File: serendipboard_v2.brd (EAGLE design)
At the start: 34.3 x 56.8 mm, 86 parts, among them IC1 TP4056, IC2 DW01A, IC3 DS3231/SO, J4 USB3076-XX-X_REVC, Q1 FS8205A, Q2 MMBT2222ALT1G, Q3 RUC002N05HZGT116, Q4 DMG3415U, Q5 MMBT2222ALT1G, Q7 RUC002N05HZGT116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

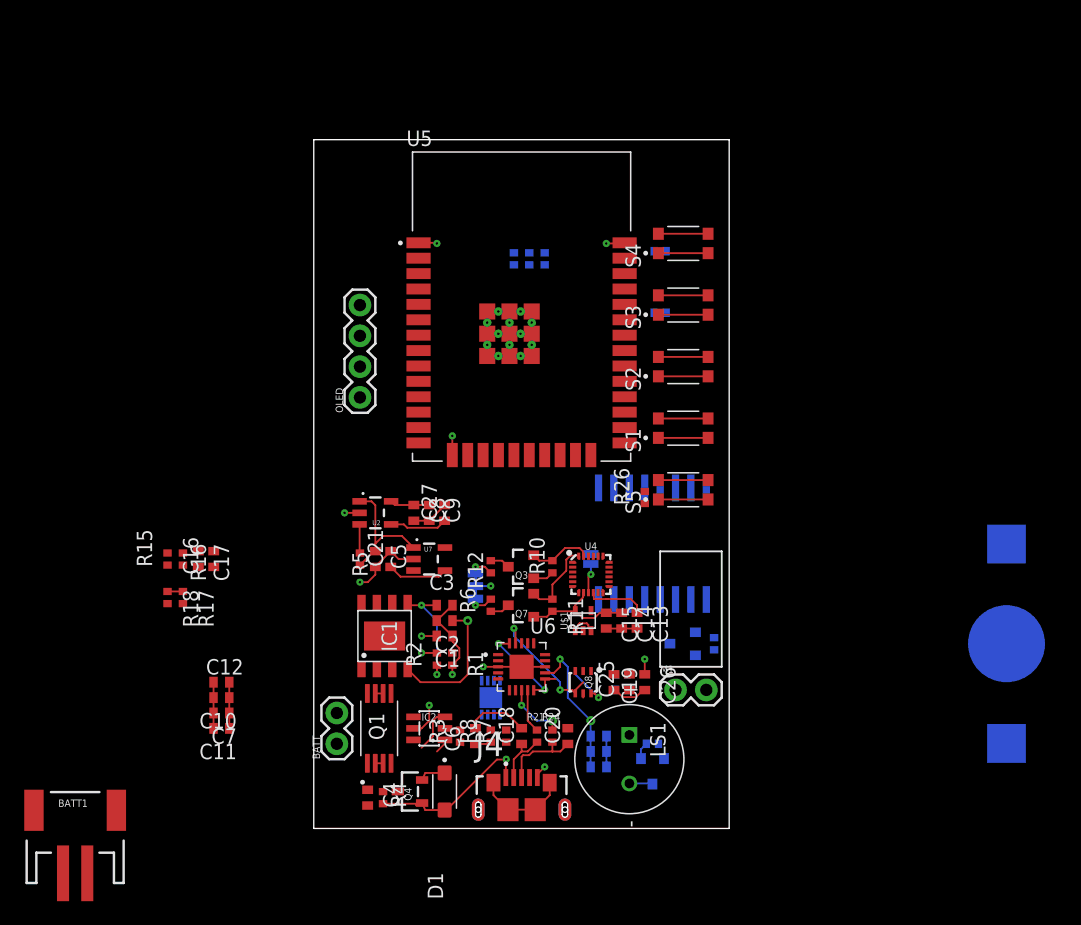
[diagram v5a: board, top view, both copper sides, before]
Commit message: Update serendipboard_v2.brd
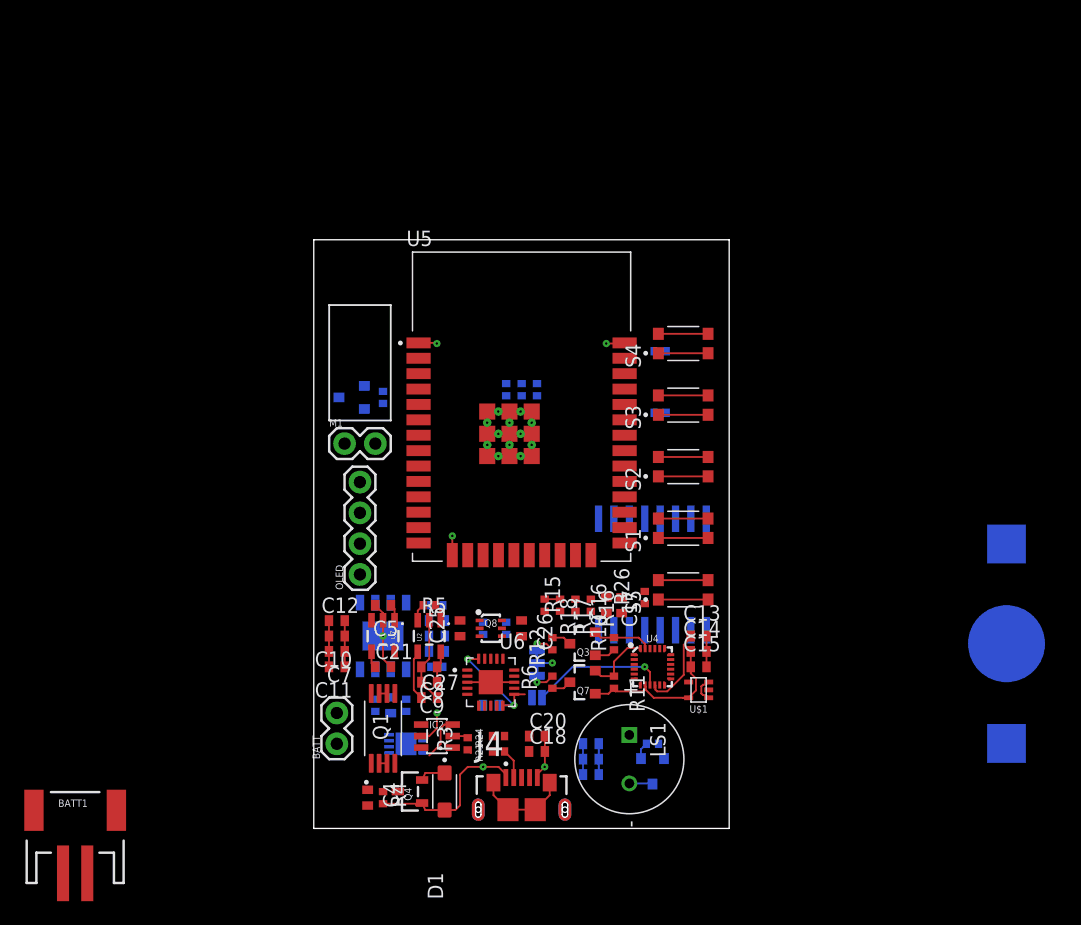
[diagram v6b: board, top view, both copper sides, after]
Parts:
- moved R13 34.0 mm to (5.71, 35.6)
- moved M1 34.0 mm to (2.54, 31.8)
- moved Q5 34.0 mm to (3.17, 35.6)
- moved C16 33.9 mm to (25.4, 18.4)
- moved C17 33.9 mm to (24.1, 18.4)
- moved R15 33.9 mm to (21.6, 18.4)
- moved R16 33.9 mm to (22.9, 18.4)
- moved R17 31.1 mm to (20.3, 18.4)
- moved R18 31.1 mm to (19.1, 18.4)
- moved C27 15.3 mm to (9.53, 10.8), turned to 0 degrees
- moved C25 14.7 mm to (12.1, 16.5)
- moved OLED 14.6 mm to (3.81, 21.0)
- moved C9 14.0 mm to (9.53, 12.1), turned to 180 degrees
- moved C8 12.8 mm to (9.53, 13.3), turned to 180 degrees
- moved R23 12.5 mm to (14.0, 16.5), turned to 270 degrees
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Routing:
- net VBUS: track 37.3 -> 16.9 mm, vias 4 -> 1
- net GND: track 68.7 -> 56.9 mm, vias 8 -> 5
- net RTS: track 10.7 -> 0.00 mm, vias 2 -> 0
- net VBAT: track 9.87 -> 0.00 mm, vias 2 -> 0
- net AD0: track 2.45 -> 11.2 mm
- net VIN: track 13.0 -> 5.14 mm
- net N$21: track 6.73 -> 0.00 mm
- net N$22: track 5.08 -> 0.00 mm, vias 2 -> 0
- net IO0: track 8.81 -> 4.10 mm, vias 2 -> 0
- net 1.8V: track 11.4 -> 15.3 mm
- net N$25: track 5.02 -> 1.36 mm
- net N$20: track 3.60 -> 0.00 mm
- net N$3: track 5.36 -> 2.83 mm, vias 3 -> 1
- net N$16: track 4.63 -> 2.46 mm
- net N$11: track 4.94 -> 6.81 mm
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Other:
- board size 34.3 x 56.8 mm -> 34.3 x 48.6 mm

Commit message: .
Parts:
- removed BATT1: (no value), SparkFun-Connectors:JST-2-SMD
- moved B1 34.1 mm to (27.3, 31.8)
- moved R28 14.1 mm to (14.6, 36.2), turned to 90 degrees
- moved R27 13.1 mm to (15.9, 36.2), turned to 90 degrees
- moved IC3 5.71 mm to (27.9, 15.2)
- moved C4 5.12 mm to (9.53, 3.17), flipped to the bottom
- moved R4 5.12 mm to (10.8, 3.17), flipped to the bottom, turned to 90 degrees
- moved R19 1.27 mm to (19.7, 36.2)
- moved R20 1.27 mm to (18.4, 36.2)
- moved R9 1.27 mm to (17.1, 36.2)
- moved LS1 0.63 mm to (26.0, 6.35)
- moved C25 0.63 mm to (12.1, 17.1)
- moved C26 0.63 mm to (17.1, 17.1)
- moved Q8 0.63 mm to (14.6, 17.1)
- moved R22 0.63 mm to (15.9, 17.1)
- moved R23 0.63 mm to (14.0, 17.1)
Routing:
- net VBUS: track 16.9 -> 13.5 mm
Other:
- board size 34.3 x 48.6 mm -> 34.3 x 48.3 mm

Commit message: Update serendipboard_v2.brd
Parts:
- moved C12 32.4 mm to (31.8, 4.45), flipped to the bottom
- moved C10 31.5 mm to (31.8, 5.71), flipped to the bottom
- moved C7 30.8 mm to (31.8, 6.99), flipped to the bottom
- moved C11 30.3 mm to (31.8, 8.26), flipped to the bottom
